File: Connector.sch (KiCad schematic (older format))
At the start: 9 parts, among them J1 776163-1, J2 Conn_02x05_Top_Bottom, J3 Conn_02x04_Top_Bottom, J4 Conn_02x04_Top_Bottom, J5 Conn_02x05_Top_Bottom

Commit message: Added bom and schematic
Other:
- note added: "Зарицкий"
- note added: "Монтажные отверстия"
- note added: "Схема электрическая принципиальная"
- moved on the sheet: H1, H2, H3, H4, J1, J2, J3, J4, J5

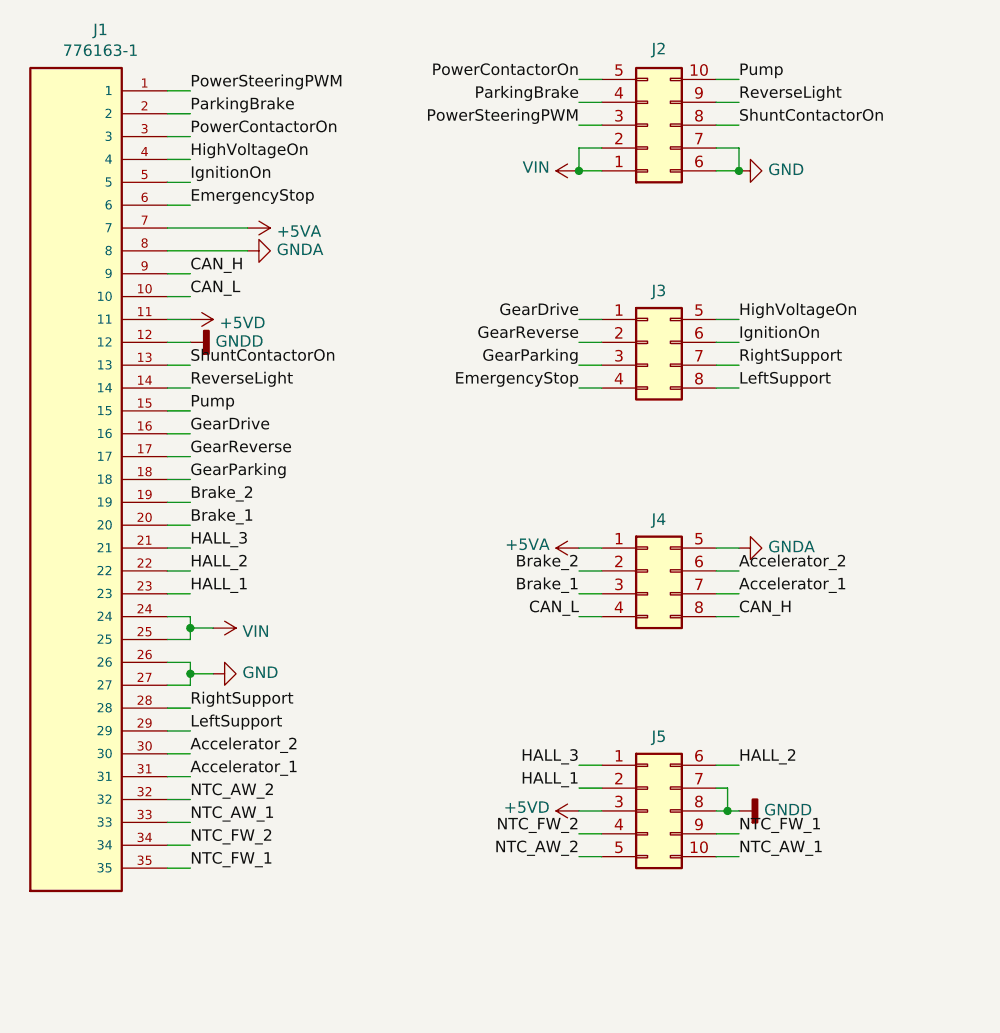
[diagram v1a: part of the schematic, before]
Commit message: Added rd_converter inputs/outputs
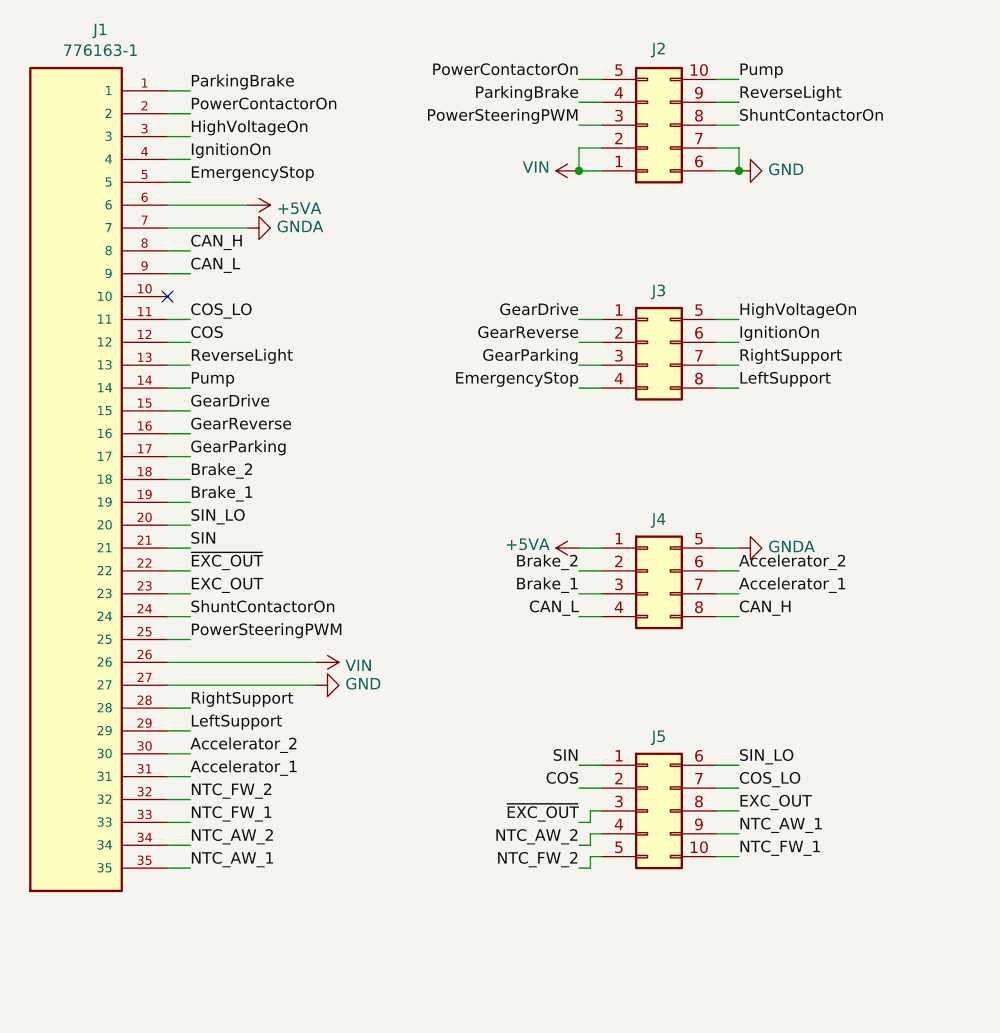
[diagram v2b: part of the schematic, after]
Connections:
- net +5VA: now also J1.6; no longer J1.7
- net Brake_1: now also J1.19; no longer J1.20
- net Brake_2: now also J1.18; no longer J1.19
- net CAN_H: now also J1.8; no longer J1.9
- net CAN_L: now also J1.9; no longer J1.10
- net EmergencyStop: now also J1.5; no longer J1.6
- net GND: no longer J1.26
- net GNDA: now also J1.7; no longer J1.8
- net GearDrive: now also J1.15; no longer J1.16
- net GearParking: now also J1.17; no longer J1.18
- net GearReverse: now also J1.16; no longer J1.17
- net HighVoltageOn: now also J1.3; no longer J1.4
- net IgnitionOn: now also J1.4; no longer J1.5
- net NTC_AW_1: now also J1.35, J5.9 (Pin_9); no longer J1.33, J5.10 (Pin_10)
- net NTC_AW_2: now also J1.34, J5.4 (Pin_4); no longer J1.32, J5.5 (Pin_5)
- net NTC_FW_1: now also J1.33, J5.10 (Pin_10); no longer J1.35, J5.9 (Pin_9)
- net NTC_FW_2: now also J1.32, J5.5 (Pin_5); no longer J1.34, J5.4 (Pin_4)
- net ParkingBrake: now also J1.1; no longer J1.2
- net PowerContactorOn: now also J1.2; no longer J1.3
- net PowerSteeringPWM: now also J1.25; no longer J1.1
- net Pump: now also J1.14; no longer J1.15
- net ReverseLight: now also J1.13; no longer J1.14
- net ShuntContactorOn: now also J1.24; no longer J1.13
- net VDD: now also J1.26; no longer J1.24, J1.25
- net +5VD renamed COS_LO
- net COS_LO: now also J5.7 (Pin_7); no longer J5.3 (Pin_3)
- removed net GNDD: J1.12, J5.7 (Pin_7), J5.8 (Pin_8)
- net HALL_1 renamed COS
- net COS: now also J1.12; no longer J1.23
- net HALL_2 renamed SIN_LO
- net SIN_LO: now also J1.20; no longer J1.22
- net HALL_3 renamed SIN
- new net EXC_OUT: J1.23, J5.8 (Pin_8)
- new net ~EXC_OUT: J1.22, J5.3 (Pin_3)
- no-connect marks 0 -> 1
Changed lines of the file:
@@
 	0    -1   -1   0
 $EndComp
-Text Label 4900 5200 2    50   ~ 0
-HALL_1
-Text Label 5600 5100 0    50   ~ 0
-HALL_2
-Text Label 4900 5100 2    50   ~ 0
-HALL_3
-$Comp
-L power:+5VD #PWR0103
-U 1 1 61093076
-P 4900 5300
-F 0 "#PWR0103" H 4900 5150 50  0001 C CNN
-F 1 "+5VD" V 4915 5428 50  0000 L CNN
-F 2 "" H 4900 5300 50  0001 C CNN
-F 3 "" H 4900 5300 50  0001 C CNN
-	1    4900 5300
-	0    -1   -1   0
-$EndComp
-$Comp
-L power:GNDD #PWR0104
-U 1 1 61093201
-P 5600 5300
-F 0 "#PWR0104" H 5600 5050 50  0001 C CNN
-F 1 "GNDD" V 5604 5190 50  0000 R CNN
-F 2 "" H 5600 5300 50  0001 C CNN
-F 3 "" H 5600 5300 50  0001 C CNN
-	1    5600 5300
-	0    -1   -1   0
-$EndComp
+Text Label 5600 5500 0    50   ~ 0
+NTC_FW_1
+Text Label 4900 5550 2    50   ~ 0
+NTC_FW_2
 Text Label 5600 5400 0    50   ~ 0
-NTC_FW_1
-Text Label 4900 5400 2    50   ~ 0
-NTC_FW_2
-Text Label 5600 5500 0    50   ~ 0
 NTC_AW_1
-Text Label 4900 5500 2    50   ~ 0
+Text Label 4900 5450 2    50   ~ 0
 NTC_AW_2
 Text Label 5600 4450 0    50   ~ 0
@@
 Text Label 5600 3150 0    50   ~ 0
 HighVoltageOn
-Text Label 3200 2650 0    50   ~ 0
+Text Label 3200 2550 0    50   ~ 0
 EmergencyStop
 Text Label 5600 4350 0    50   ~ 0
@@
 	5500 2300 5600 2300
 Wire Wire Line
-	5000 5100 4900 5100
-Wire Wire Line
-	4900 5200 5000 5200
-Wire Wire Line
-	5000 5300 4900 5300
-Wire Wire Line
-	5500 5100 5600 5100
-Wire Wire Line
-	5500 5400 5600 5400
-Wire Wire Line
-	5500 5500 5600 5500
-Wire Wire Line
-	5000 5400 4900 5400
-Wire Wire Line
-	5000 5500 4900 5500
-Wire Wire Line
-	5500 5300 5550 5300
-Wire Wire Line
 	4900 4150 5000 4150
 Wire Wire Line
@@
 	1    0    0    -1
 $EndComp
-Wire Wire Line
-	5500 5200 5550 5200
-Wire Wire Line
-	5550 5200 5550 5300
-Connection ~ 5550 5300
-Wire Wire Line
-	5550 5300 5600 5300
+Text Label 3200 4550 0    50   ~ 0
+PowerSteeringPWM
+Text Label 3200 2250 0    50   ~ 0
+PowerContactorOn
 Text Label 3200 2150 0    50   ~ 0
-PowerSteeringPWM
-Text Label 3200 2350 0    50   ~ 0
-PowerContactorOn
-Text Label 3200 2250 0    50   ~ 0
 ParkingBrake
 $Comp
 L power:GND #PWR0106
 U 1 1 6120E0B5
-P 3300 4700
-F 0 "#PWR0106" H 3300 4450 50  0001 C CNN
-F 1 "GND" V 3305 4572 50  0000 R CNN
-F 2 "" H 3300 4700 50  0001 C CNN
-F 3 "" H 3300 4700 50  0001 C CNN
-	1    3300 4700
+P 3750 4750
+F 0 "#PWR0106" H 3750 4500 50  0001 C CNN
+F 1 "GND" V 3755 4622 50  0000 R CNN
+F 2 "" H 3750 4750 50  0001 C CNN
+F 3 "" H 3750 4750 50  0001 C CNN
+	1    3750 4750
 	0    -1   -1   0
 $EndComp
+Text Label 3200 3350 0    50   ~ 0
+ReverseLight
+Text Label 3200 4450 0    50   ~ 0
+ShuntContactorOn
 Text Label 3200 3450 0    50   ~ 0
-ReverseLight
-Text Label 3200 3350 0    50   ~ 0
-ShuntContactorOn
-Text Label 3200 3550 0    50   ~ 0
 Pump
-Wire Wire Line
-	3100 4450 3200 4450
-Wire Wire Line
-	3200 4550 3100 4550
-Wire Wire Line
-	3100 4650 3200 4650
-Wire Wire Line
-	3100 4750 3200 4750
-Wire Wire Line
-	3200 4450 3200 4500
-Wire Wire Line
-	3200 4650 3200 4700
 $Comp
 L Connector-rescue:VIN-MyLibrary #PWR0105
 U 1 1 6120D1A1
-P 3300 4500
-F 0 "#PWR0105" H 3300 4350 50  0001 C CNN
-F 1 "VIN" V 3315 4628 50  0000 L CNN
-F 2 "" H 3300 4500 50  0001 C CNN
-F 3 "" H 3300 4500 50  0001 C CNN
-	1    3300 4500
+P 3750 4650
+F 0 "#PWR0105" H 3750 4500 50  0001 C CNN
+F 1 "VIN" V 3765 4778 50  0000 L CNN
+F 2 "" H 3750 4650 50  0001 C CNN
+F 3 "" H 3750 4650 50  0001 C CNN
+	1    3750 4650
 	0    1    1    0
 $EndComp
-Wire Wire Line
-	3300 4500 3200 4500
-Connection ~ 3200 4500
-Wire Wire Line
-	3200 4500 3200 4550
-Wire Wire Line
-	3300 4700 3200 4700
-Connection ~ 3200 4700
-Wire Wire Line
-	3200 4700 3200 4750
 Wire Wire Line
 	3100 3350 3200 3350
@@
 Text Label 4900 3150 2    50   ~ 0
 GearDrive
-Text Label 3200 3850 0    50   ~ 0
+Text Label 3200 3750 0    50   ~ 0
 GearParking
-Text Label 3200 3750 0    50   ~ 0
+Text Label 3200 3650 0    50   ~ 0
 GearReverse
-Text Label 3200 3650 0    50   ~ 0
+Text Label 3200 3550 0    50   ~ 0
 GearDrive
 Wire Wire Line
@@
 Wire Wire Line
 	3100 4950 3200 4950
-Text Label 3200 2550 0    50   ~ 0
+Text Label 3200 2450 0    50   ~ 0
 IgnitionOn
-Text Label 3200 2450 0    50   ~ 0
+Text Label 3200 2350 0    50   ~ 0
 HighVoltageOn
 Wire Wire Line
@@
 Wire Wire Line
 	3100 2550 3200 2550
-Wire Wire Line
-	3100 2650 3200 2650
 Text Label 4900 3450 2    50   ~ 0
 EmergencyStop
 Text Label 3200 2950 0    50   ~ 0
-CAN_H
-Text Label 3200 3050 0    50   ~ 0
 CAN_L
 Wire Wire Line
+	3100 2850 3200 2850
+Wire Wire Line
 	3100 2950 3200 2950
-Wire Wire Line
-	3100 3050 3200 3050
-$Comp
-L power:+5VA #PWR0109
-U 1 1 612628C1
-P 3450 2750
-F 0 "#PWR0109" H 3450 2600 50  0001 C CNN
-F 1 "+5VA" V 3465 2878 50  0000 L CNN
-F 2 "" H 3450 2750 50  0001 C CNN
-F 3 "" H 3450 2750 50  0001 C CNN
-	1    3450 2750
-	0    1    1    0
-$EndComp
-$Comp
-L power:GNDA #PWR0110
-U 1 1 61262A94
-P 3450 2850
-F 0 "#PWR0110" H 3450 2600 50  0001 C CNN
-F 1 "GNDA" V 3455 2722 50  0000 R CNN
-F 2 "" H 3450 2850 50  0001 C CNN
-F 3 "" H 3450 2850 50  0001 C CNN
-	1    3450 2850
-	0    -1   -1   0
-$EndComp
-Wire Wire Line
-	3100 2750 3450 2750
-Wire Wire Line
-	3100 2850 3450 2850
+Text Label 3200 3850 0    50   ~ 0
+Brake_2
 Text Label 3200 3950 0    50   ~ 0
-Brake_2
-Text Label 3200 4050 0    50   ~ 0
 Brake_1
 Wire Wire Line
 	3100 3950 3200 3950
-Wire Wire Line
-	3100 4050 3200 4050
-Text Label 3200 5050 0    50   ~ 0
-Accelerator_2
 Text Label 3200 5150 0    50   ~ 0
 Accelerator_1
@@
 Wire Wire Line
 	3100 5150 3200 5150
-Wire Wire Line
-	3100 3250 3200 3250
-$Comp
-L power:GNDD #PWR0111
-U 1 1 6127FE45
-P 3200 3250
-F 0 "#PWR0111" H 3200 3000 50  0001 C CNN
-F 1 "GNDD" V 3204 3140 50  0000 R CNN
-F 2 "" H 3200 3250 50  0001 C CNN
-F 3 "" H 3200 3250 50  0001 C CNN
-	1    3200 3250
-	0    -1   -1   0
-$EndComp
-Wire Wire Line
-	3100 3150 3200 3150
-$Comp
-L power:+5VD #PWR0112
-U 1 1 6127FAC8
-P 3200 3150
-F 0 "#PWR0112" H 3200 3000 50  0001 C CNN
-F 1 "+5VD" V 3215 3278 50  0000 L CNN
-F 2 "" H 3200 3150 50  0001 C CNN
-F 3 "" H 3200 3150 50  0001 C CNN
-	1    3200 3150
-	0    1    1    0
-$EndComp
-Text Label 3200 4150 0    50   ~ 0
-HALL_3
-Text Label 3200 4250 0    50   ~ 0
-HALL_2
-Text Label 3200 4350 0    50   ~ 0
-HALL_1
-Wire Wire Line
-	3100 4150 3200 4150
-Wire Wire Line
-	3100 4250 3200 4250
-Wire Wire Line
-	3100 4350 3200 4350
-Text Label 3200 5450 0    50   ~ 0
-NTC_FW_2
-Text Label 3200 5550 0    50   ~ 0
-NTC_FW_1
-Text Label 3200 5250 0    50   ~ 0
-NTC_AW_2
-Text Label 3200 5350 0    50   ~ 0
-NTC_AW_1
-Wire Wire Line
-	3100 5250 3200 5250
-Wire Wire Line
-	3100 5350 3200 5350
-Wire Wire Line
-	3100 5450 3200 5450
-Wire Wire Line
-	3100 5550 3200 5550
 Text Label 5600 2100 0    50   ~ 0
 Pump
@@
 Text Notes 3735 10865 0    67   ~ 0
 Схема электрическая принципиальная
+Wire Wire Line
+	3750 4750 3100 4750
+Wire Wire Line
+	3100 4650 3750 4650
+Wire Wire Line
+	3100 4450 3200 4450
+Wire Wire Line
+	3200 4550 3100 4550
+Text Label 3200 5050 0    50   ~ 0
+Accelerator_2
+Wire Wire Line
+	3100 2750 3450 2750
+Wire Wire Line
+	3100 2650 3450 2650
+$Comp
+L power:GNDA #PWR0110
+U 1 1 61262A94
+P 3450 2750
+F 0 "#PWR0110" H 3450 2500 50  0001 C CNN
+F 1 "GNDA" V 3455 2622 50  0000 R CNN
+F 2 "" H 3450 2750 50  0001 C CNN
+F 3 "" H 3450 2750 50  0001 C CNN
+	1    3450 2750
+	0    -1   -1   0
+$EndComp
+$Comp
+L power:+5VA #PWR0109
+U 1 1 612628C1
+P 3450 2650
+F 0 "#PWR0109" H 3450 2500 50  0001 C CNN
+F 1 "+5VA" V 3465 2778 50  0000 L CNN
+F 2 "" H 3450 2650 50  0001 C CNN
+F 3 "" H 3450 2650 50  0001 C CNN
+	1    3450 2650
+	0    1    1    0
+$EndComp
+Text Label 3200 2850 0    50   ~ 0
+CAN_H
+Text Label 4900 5350 2    50   ~ 0
+~EXC_OUT
+Wire Wire Line
+	3100 4350 3200 4350
+Wire Wire Line
+	3100 4250 3200 4250
+Wire Wire Line
+	3100 4150 3200 4150
+Wire Wire Line
+	3100 5250 3200 5250
+Wire Wire Line
+	3100 5350 3200 5350
+Wire Wire Line
+	3100 5450 3200 5450
+Wire Wire Line
+	3100 5550 3200 5550
+Text Label 3200 5350 0    50   ~ 0
+NTC_FW_1
+Text Label 3200 5250 0    50   ~ 0
+NTC_FW_2
+Text Label 3200 5550 0    50   ~ 0
+NTC_AW_1
+Text Label 3200 5450 0    50   ~ 0
+NTC_AW_2
+NoConn ~ 3100 3050
+Text Label 5600 5300 0    50   ~ 0
+EXC_OUT
+Wire Wire Line
+	4900 5350 4950 5350
+Wire Wire Line
+	4950 5350 4950 5300
+Wire Wire Line
+	4950 5300 5000 5300
+Wire Wire Line
+	5000 5400 4950 5400
+Wire Wire Line
+	4950 5400 4950 5450
+Wire Wire Line
+	4950 5450 4900 5450
+Wire Wire Line
+	5000 5500 4950 5500
+Wire Wire Line
+	4950 5500 4950 5550
+Wire Wire Line
+	4950 5550 4900 5550
+Wire Wire Line
+	5500 5400 5600 5400
+Wire Wire Line
+	5500 5500 5600 5500
+Wire Wire Line
+	5500 5300 5600 5300
+Text Label 5600 5200 0    50   ~ 0
+COS_LO
+Text Label 5600 5100 0    50   ~ 0
+SIN_LO
+Wire Wire Line
+	4900 5200 5000 5200
+Wire Wire Line
+	4900 5100 5000 5100
+Text Label 4900 5200 2    50   ~ 0
+COS
+Text Label 4900 5100 2    50   ~ 0
+SIN
+Wire Wire Line
+	5600 5200 5500 5200
+Wire Wire Line
+	5600 5100 5500 5100
+Text Label 3200 4250 0    50   ~ 0
+~EXC_OUT
+Text Label 3200 4350 0    50   ~ 0
+EXC_OUT
+Text Label 3200 3150 0    50   ~ 0
+COS_LO
+Text Label 3200 3250 0    50   ~ 0
+COS
+Wire Wire Line
+	3200 3150 3100 3150
+Wire Wire Line
+	3200 3250 3100 3250
+Text Label 3200 4150 0    50   ~ 0
+SIN
+Text Label 3200 4050 0    50   ~ 0
+SIN_LO
+Wire Wire Line
+	3100 4050 3200 4050
 $EndSCHEMATC

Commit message: RevC
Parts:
- J1: symbol 776163-1:776163-1 -> Connector-rescue:776163-1-776163-1
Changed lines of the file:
@@
 $EndDescr
 $Comp
-L 776163-1:776163-1 J1
+L Connector-rescue:776163-1-776163-1 J1
 U 1 1 60EEA6B9
 P 2700 3850
